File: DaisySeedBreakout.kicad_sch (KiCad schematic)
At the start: 10 parts, among them J1 STX-3000, J2 Conn_02x08, J3 STX-3000, J5 Conn_02x08, J6 Conn_02x08

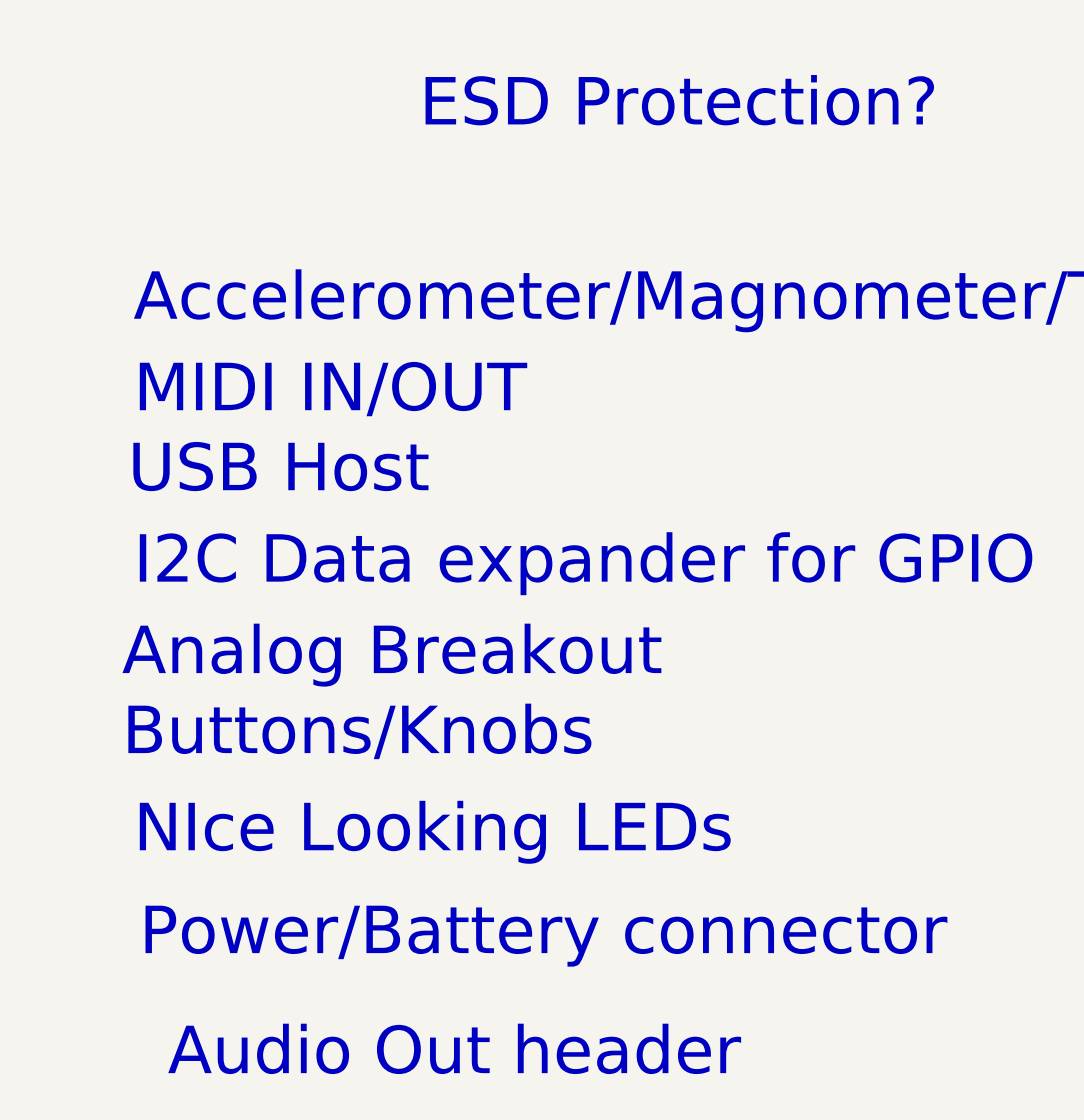
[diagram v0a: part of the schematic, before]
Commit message: Fixed ultralibrarian library with capital letter difference
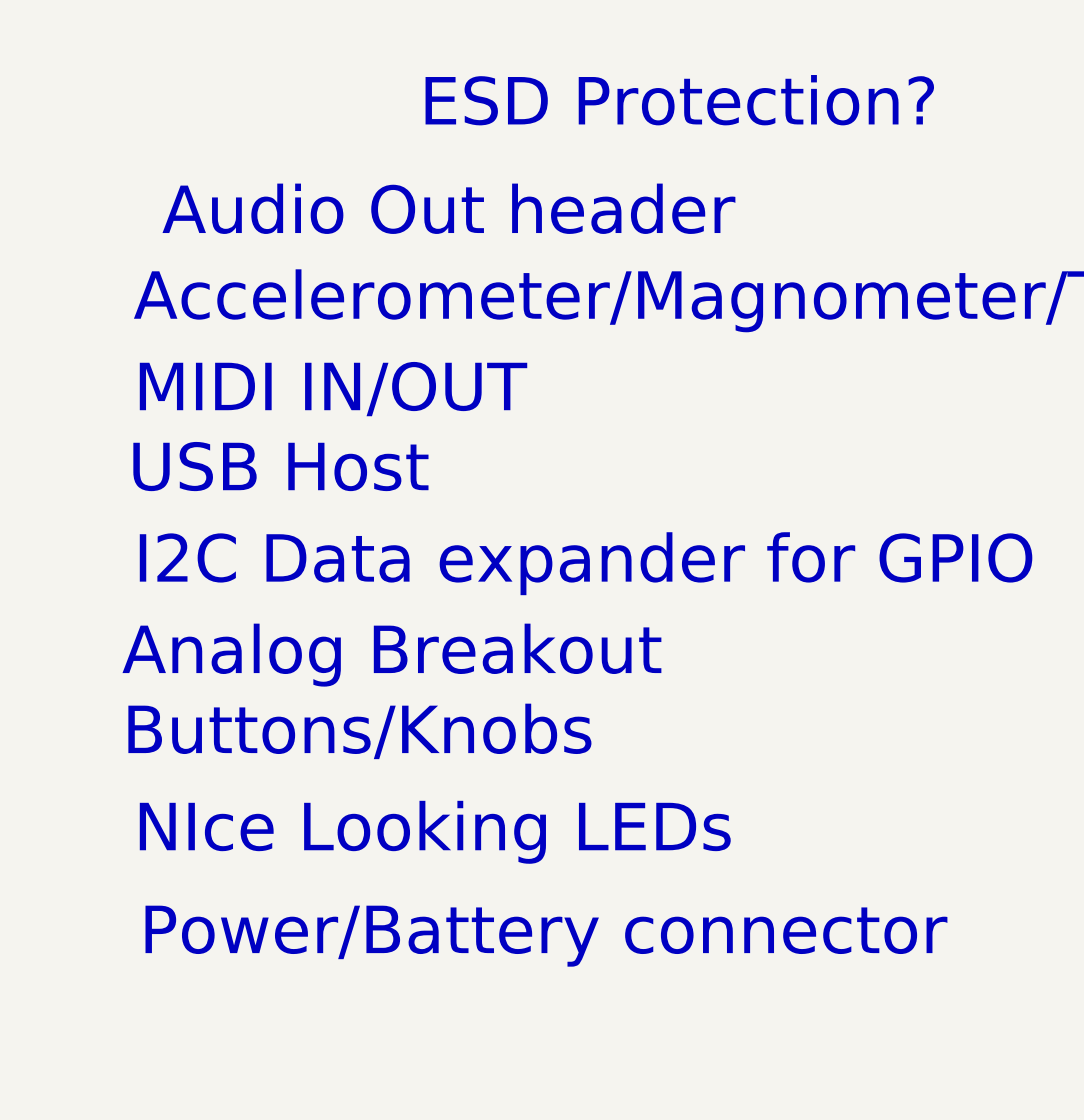
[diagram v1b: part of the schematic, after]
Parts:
- J1, J3: footprint UltraLibrarian:STX-3000_KYC -> Ultralibrarian:STX-3000_KYC
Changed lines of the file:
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@@
     (effects (font (size 1.27 1.27)) (justify left bottom))
   )
-  (text "Audio Out header" (at 89.535 276.225 0)
+  (text "Audio Out header" (at 88.9 182.88 0)
     (effects (font (size 5.27 5.27)) (justify left bottom))
   )
@@
       (effects (font (size 1.524 1.524)))
     )
-    (property "Footprint" "UltraLibrarian:STX-3000_KYC" (at 35.56 113.411 0)
+    (property "Footprint" "Ultralibrarian:STX-3000_KYC" (at 35.56 113.411 0)
       (effects (font (size 1.524 1.524)) hide)
     )
@@
       (effects (font (size 1.524 1.524)))
     )
-    (property "Footprint" "UltraLibrarian:STX-3000_KYC" (at 35.56 89.916 0)
+    (property "Footprint" "Ultralibrarian:STX-3000_KYC" (at 35.56 89.916 0)
       (effects (font (size 1.524 1.524)) hide)
     )

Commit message: added knob headers, MIDI in header
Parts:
- removed J6: Conn_02x08, Connector_PinHeader_2.54mm:PinHeader_2x08_P2.54mm_Vertical, symbol 4ms_Connector:Conn_02x08
- added C10, C25, C26, C27, C28, C7, C9: 0.1uF, Capacitor_SMD:C_0402_1005Metric, symbol Device:C_Small
- added C29, C30: 0.1uF, Capacitor_SMD:C_0402_1005Metric, symbol Device:C
- added C31: 0.1uF, Capacitor_SMD:C_0603_1608Metric, symbol Device:C_Small
- added J10, J11, J12, J13, J14, J6, J7, J8, J9: Conn_01x03, Connector_PinHeader_2.54mm:PinHeader_1x03_P2.54mm_Vertical, symbol 4ms_Connector:Conn_01x03
- added J15: Conn_02x08, Connector_PinHeader_2.54mm:PinHeader_2x08_P2.54mm_Vertical, symbol 4ms_Connector:Conn_02x08
- added R78, R79, R80, R81, R82, R83, R84: 1k, Resistor_SMD:R_0402_1005Metric, symbol Device:R_US
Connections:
- net +5V_ISO: now also C29.1, C30.1, J10.2 (Pin_2), J11.2 (Pin_2), J12.2 (Pin_2), J13.2 (Pin_2), J14.2 (Pin_2), J7.2 (Pin_2), J8.2 (Pin_2), J9.2 (Pin_2)
- net +9V: now also C31.1, J6.2 (Pin_2)
- net Audio Out/AUDIO_OUT_L_EXT: now also J6.3 (Pin_3)
- net GND: now also C10.2, C25.2, C26.2, C27.2, C28.2, C29.2, C30.2, C31.2, C7.2, C9.2, J10.1 (Pin_1), J11.1 (Pin_1), J12.1 (Pin_1), J13.1 (Pin_1), J14.1 (Pin_1), J15.10 (GND), J15.12 (GND), J15.14 (-12V), J15.16 (P16), J15.2 (P2), J15.4 (P4), J15.6 (P6), J15.8 (+12V), J6.1 (Pin_1), J7.1 (Pin_1), J8.1 (Pin_1), J9.1 (Pin_1)
- net I2C 24 GPIO/A0: now also J15.1 (P1); no longer J2.1 (P1)
- net I2C 24 GPIO/A1: now also J15.3 (P3); no longer J2.3 (P3)
- net I2C 24 GPIO/A2: now also J15.5 (+12V); no longer J2.5 (+12V)
- net I2C 24 GPIO/A3: now also J15.7 (12V); no longer J2.7 (12V)
- net I2C 24 GPIO/A4: now also J15.9 (GND); no longer J2.9 (GND)
- net I2C 24 GPIO/A5: now also J15.11 (GND); no longer J2.11 (GND)
- net I2C 24 GPIO/A6: now also J15.13 (-12); no longer J2.13 (-12)
- net I2C 24 GPIO/A7: now also J15.15 (-12V); no longer J2.15 (-12V)
- net I2C 24 GPIO/B0: now also J2.1 (P1); no longer J5.1 (P1)
- net I2C 24 GPIO/B1: now also J2.3 (P3); no longer J5.3 (P3)
- net I2C 24 GPIO/B2: now also J2.5 (+12V); no longer J5.5 (+12V)
- net I2C 24 GPIO/B3: now also J2.7 (12V); no longer J5.7 (12V)
- net I2C 24 GPIO/B4: now also J2.9 (GND); no longer J5.9 (GND)
- net I2C 24 GPIO/B5: now also J2.11 (GND); no longer J5.11 (GND)
- net I2C 24 GPIO/B6: now also J2.13 (-12); no longer J5.13 (-12)
- net I2C 24 GPIO/B7: now also J2.15 (-12V); no longer J5.15 (-12V)
- net I2C 24 GPIO/C0: now also J5.1 (P1)
- net I2C 24 GPIO/C1: now also J5.3 (P3)
- net I2C 24 GPIO/C2: now also J5.5 (+12V)
- net I2C 24 GPIO/C3: now also J5.7 (12V)
- net I2C 24 GPIO/C4: now also J5.9 (GND)
- net I2C 24 GPIO/C5: now also J5.11 (GND)
- net I2C 24 GPIO/C6: now also J5.13 (-12)
- net I2C 24 GPIO/C7: now also J5.15 (-12V)
- net MIDI_UART_TX: now reaches A1.14 (USART1_TX)
- net MIDI_UART_RX: now reaches A1.15 (USART1_RX)
- net MIDI_UART_RX: now also J7.3 (Pin_3)
- net AI0: now reaches A1.22 (ADC_0)
- net AI0: now also C7.1, R78.1
- net AI1: now reaches A1.23 (ADC_1)
- net AI1: now also C9.1, R79.1
- net AI2: now reaches A1.24 (ADC_2)
- net AI2: now also C10.1, R80.1
- net AI3: now reaches A1.25 (ADC_3)
- net AI3: now also C25.1, R81.1
- net AI4: now reaches A1.26 (ADC_4)
- net AI4: now also C26.1, R82.1
- net AI5: now reaches A1.27 (ADC_5)
- net AI5: now also C27.1, R83.1
- net AI6: now reaches A1.28 (ADC_6)
- net AI6: now also C28.1, R84.1
- new net: J12.3 (Pin_3), R82.2
- new net: J9.3 (Pin_3), R79.2
- new net: J14.3 (Pin_3), R84.2
- new net: J11.3 (Pin_3), R81.2
- new net: J10.3 (Pin_3), R80.2
- new net: J13.3 (Pin_3), R83.2
- new net: J8.3 (Pin_3), R78.2
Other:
- note added: "Analog In connectors EG: Knobs"
- note added: "Header for a speaker"
- note added: "MIDI IN Header Goes to MIDI connector board."
- note added: "MIDI OUT Header Goes to MIDI connector board."
- note added: "Time constant of 0.1ms"

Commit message: added double high audio jack
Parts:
- removed J1: STX-3000, Ultralibrarian:STX-3000_KYC, symbol Ultralibrarian:STX-3000
- added C32, C33: 0.1uF, Capacitor_SMD:C_0603_1608Metric, symbol Device:C_Small
- added D1: D_Schottky, Diode_SMD:D_0402_1005Metric, symbol Device:D_Schottky_Small
- added J1, J18: ~, Ultralibrarian:STX-4235-3-3-N, symbol Ultralibrarian_modified_symbols:STX-4235-3-3-N
- added J16, J17, J19: STX-3000, Ultralibrarian:STX-3000_KYC, symbol Ultralibrarian:STX-3000
- added R85, R90, R92: 220, Resistor_SMD:R_0402_1005Metric, symbol Device:R_US
- added R86, R87, R91, R93: SPARE, Resistor_SMD:R_0402_1005Metric, symbol Device:R_US
- added R88: 0, Resistor_SMD:R_0402_1005Metric, symbol Device:R_US
- added R89: 270, Resistor_SMD:R_0402_1005Metric, symbol Device:R_US
- added U2: H11L1M, digikey-footprints:DIP-6_W7.62mm, symbol dk_Optoisolators-Logic-Output:H11L1M
- added U4: SN74AHCT1G125_DCK_5, DCK5, symbol SN74AHCT1G125DCKR:SN74AHCT1G125_DCK_5
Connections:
- net +3.3V: now also C32.1, R89.2, U2.6 (VCC)
- net +5V_ISO: now also C33.1, R90.1, R91.1, U4.5 (VCC)
- net Audio In Sum/AUDIO_IN_L_CONN: now also J18.5B
- net Audio In Sum/AUDIO_IN_R_CONN: now also J18.2B
- net Audio Out/AUDIO_OUT_L_EXT: now also J18.5A; no longer J3.3
- net Audio Out/AUDIO_OUT_R_EXT: now also J18.2A; no longer J3.2
- net GND: now also C32.2, C33.2, J1.1B, J18.1A, J18.1B, U2.5 (GND), U4.1 (*OE), U4.3 (GND); no longer J3.1
- net MIDI_UART_RX: now also R89.1, U2.4 (VO)
- net MIDI_UART_TX: now also U4.2 (A)
- new net: D1.2 (A), R86.1, R88.1, U2.2
- new net: J1.2B, R87.2, R88.2
- new net: R92.1, R93.1, U4.4 (Y)
- new net: R90.2, R93.2
- new net: R91.2, R92.2
- new net: J1.5B, R85.2, R86.2
- new net: D1.1 (K), R85.1, R87.1, U2.1
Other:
- note added: "Audio In"
- note added: "Audio Out"
- note added: "MIDI IN"
- note added: "MIDI OUT"
- note added: "Microphone"
- note added: "Verify MIDI Out to 3.5mm connections."
- note removed: "Audio In/Out/Microphone"
- moved on the sheet: C10, C25, C26, C27, C28, C29, C30, C7, C9, J10, J11, J12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

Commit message: adding 3d models
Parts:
- removed C33: 0.1uF, Capacitor_SMD:C_0603_1608Metric, symbol Device:C_Small
- removed R92: 220, Resistor_SMD:R_0402_1005Metric, symbol Device:R_US
- removed R93: SPARE, Resistor_SMD:R_0402_1005Metric, symbol Device:R_US
- removed U4: SN74AHCT1G125_DCK_5, DCK5, symbol SN74AHCT1G125DCKR:SN74AHCT1G125_DCK_5
- C10, C25, C27, C28, C7, C9: value 0.1uF -> SPARE
- R90: value 220 -> 10
- R91: value SPARE -> 33
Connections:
- net +5V_ISO: no longer R90.1
- net GND: now also J1.1A
- net MIDI_UART_TX: now also R90.1
- net at R90.2: now also J1.2A
- net at R91.2: now also J1.5A
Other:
- note added: "SPARE = Do not populate. Optional filter caps for analog."
- note removed: "Analog Breakout"
- note removed: "Audio Out header"
- note removed: "Buttons/Knobs"
- note removed: "I2C Data expander for GPIO"
- note removed: "MIDI IN/OUT"
- note removed: "Time constant of 0.1ms"
- note removed: "Verify MIDI Out to 3.5mm connections."
- moved on the sheet: R90

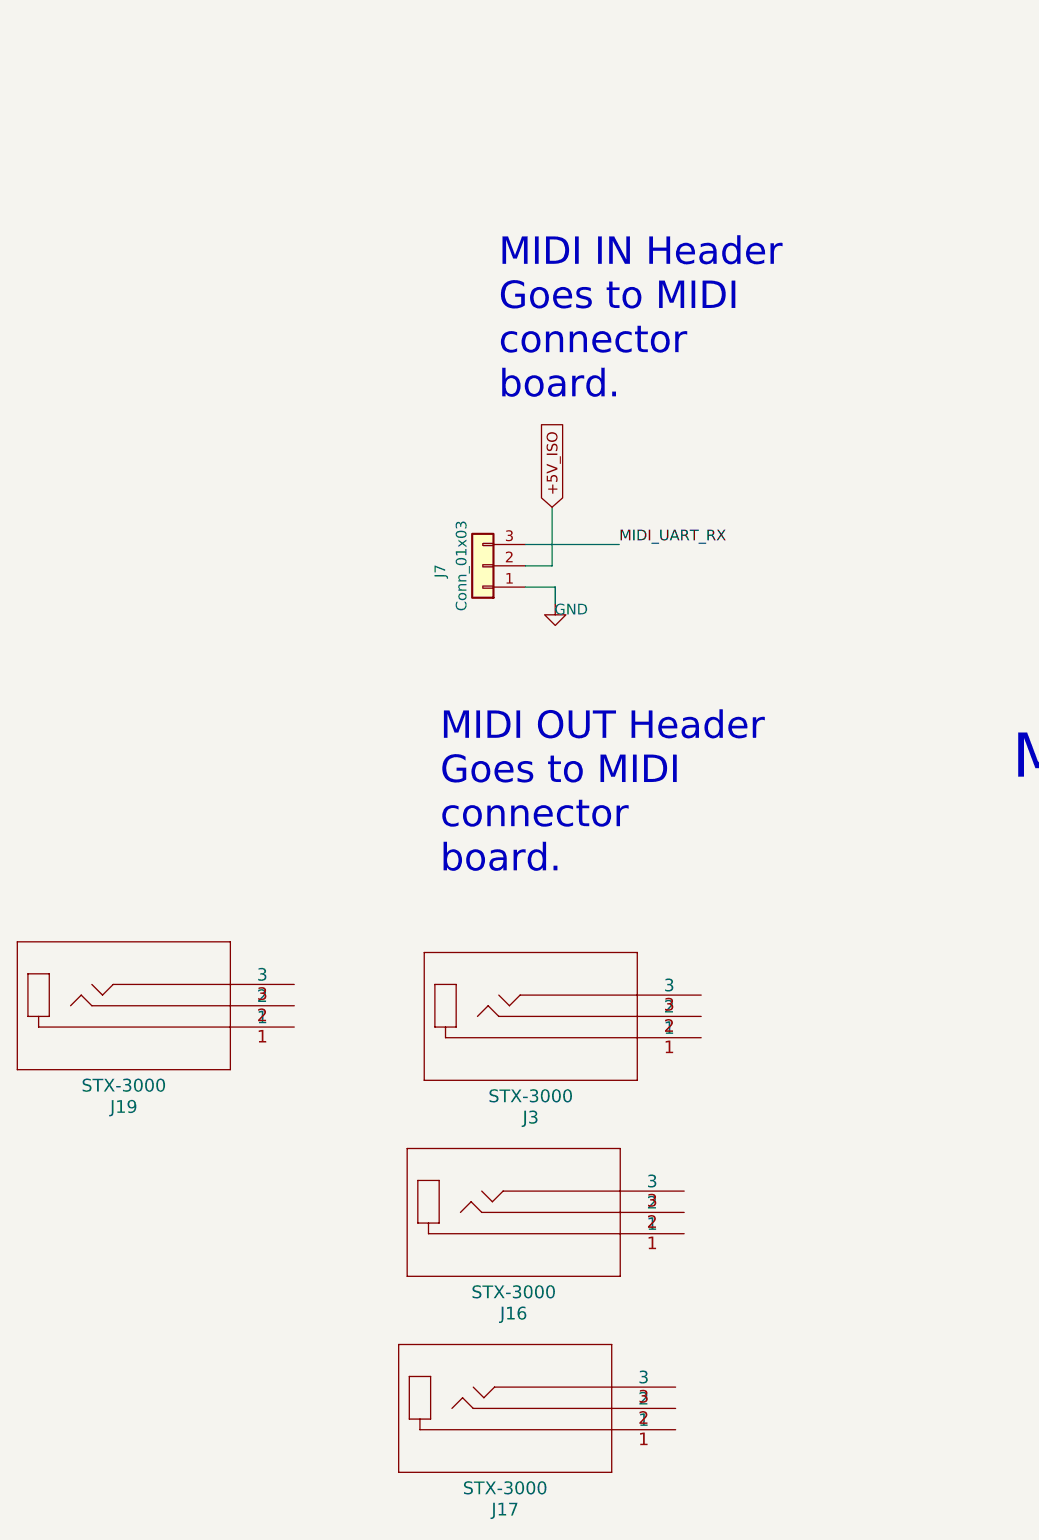
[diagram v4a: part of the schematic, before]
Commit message: adding mono connectors, CV, and gate as well
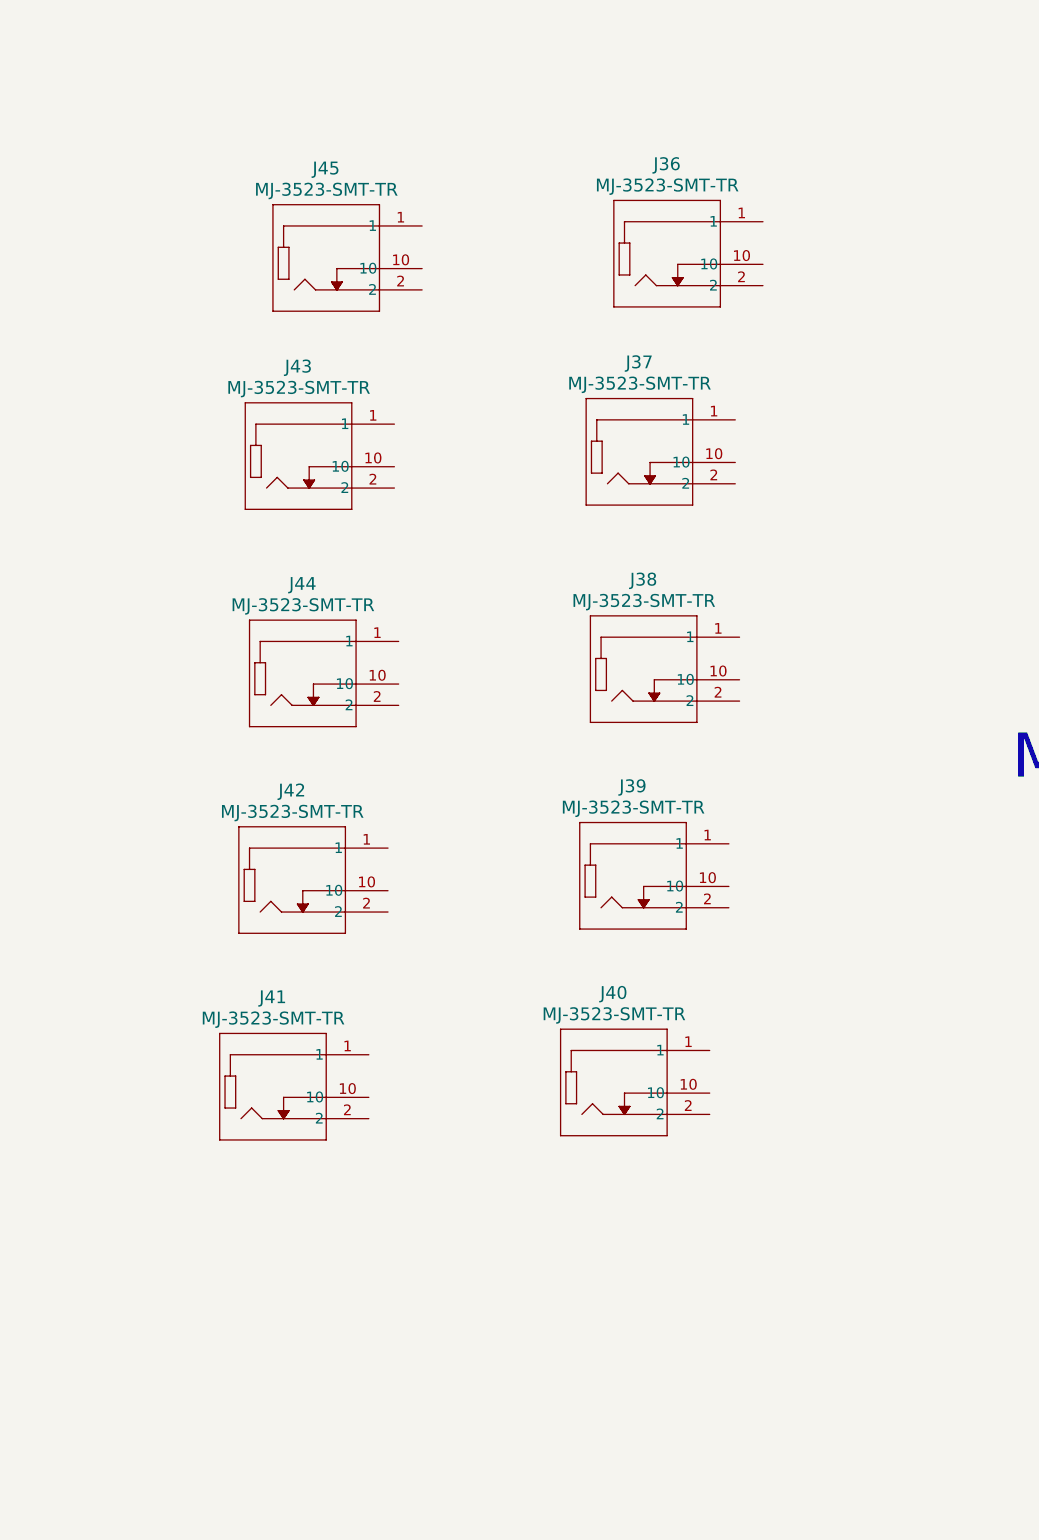
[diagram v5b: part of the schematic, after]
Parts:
- removed J16, J17, J19, J3: STX-3000, Ultralibrarian:STX-3000_KYC, symbol Ultralibrarian:STX-3000
- removed J7: Conn_01x03, Connector_PinHeader_2.54mm:PinHeader_1x03_P2.54mm_Vertical, symbol 4ms_Connector:Conn_01x03
- added J36, J37, J38, J39, J40, J41, J42, J43, J44, J45: MJ-3523-SMT-TR, SurfaceMountAudiofootprints:MJ-3523-SMT-TR, symbol 2023-09-25_23-43-35:MJ-3523-SMT-TR
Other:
- note removed: "MIDI IN Header Goes to MIDI connector board."
- note removed: "MIDI OUT Header Goes to MIDI connector board."
